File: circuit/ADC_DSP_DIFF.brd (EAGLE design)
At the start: 61 x 76.8 mm, 79 parts, among them IC1 REG1117, IC3 STM32F40XRXT6, IC4 CS4272, Q1 8MHz, Q2 24.576MHz

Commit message: - скомпилировали под Linux
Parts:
- moved C21 8.89 mm to (12.7, 27.9), flipped to the bottom
- moved C23 8.89 mm to (12.7, 25.4), flipped to the bottom
- moved C3 8.89 mm to (12.7, 33.0), flipped to the bottom
- moved C4 8.89 mm to (12.7, 30.5), flipped to the bottom
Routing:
- net GND: track 438.3 -> 418.8 mm
- net N$46: track 3.81 -> 0.00 mm
- net N$43: track 3.81 -> 0.00 mm
- net SW_A: track 9.08 -> 6.45 mm, vias 1 -> 0
- net N$45: track 2.54 -> 0.00 mm
- net N$44: track 2.54 -> 0.00 mm
- net N$27: track 2.54 -> 0.00 mm
- net N$25: track 2.54 -> 0.00 mm
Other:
- board size 61 x 76.8 mm -> 50 x 76.8 mm
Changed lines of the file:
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@@
 <grid distance="0.635" unitdist="mm" unit="mm" style="lines" multiple="1" display="no" altdistance="0.125" altunitdist="mm" altunit="mm"/>
 <layers>
-<layer number="1" name="Top" color="4" fill="1" visible="yes" active="yes"/>
+<layer number="1" name="Top" color="4" fill="1" visible="no" active="yes"/>
 <layer number="16" name="Bottom" color="1" fill="1" visible="yes" active="yes"/>
 <layer number="17" name="Pads" color="2" fill="1" visible="yes" active="yes"/>
@@
 <board>
 <plain>
-<wire x1="0" y1="0" x2="60.95" y2="0" width="0" layer="20"/>
-<wire x1="60.95" y1="0" x2="60.95" y2="76.825" width="0" layer="20"/>
-<wire x1="60.95" y1="76.825" x2="0" y2="76.825" width="0" layer="20"/>
+<wire x1="0" y1="0" x2="50" y2="0" width="0" layer="20"/>
+<wire x1="50" y1="0" x2="50" y2="76.825" width="0" layer="20"/>
+<wire x1="50" y1="76.825" x2="0" y2="76.825" width="0" layer="20"/>
 <wire x1="0" y1="76.825" x2="0" y2="0" width="0" layer="20"/>
 </plain>
@@
 <attribute name="OC_FARNELL" value="unknown" x="8.255" y="29.21" size="1.778" layer="28" rot="MR270" display="off"/>
 </element>
-<element name="C3" library="rcl" package="C0805" value="1n" x="3.81" y="33.02" rot="R180"/>
-<element name="C4" library="rcl" package="C0805" value="1n" x="3.81" y="30.48" rot="R180"/>
-<element name="C21" library="rcl" package="C0805" value="1n" x="3.81" y="27.94" rot="R180"/>
-<element name="C23" library="rcl" package="C0805" value="1n" x="3.81" y="25.4" rot="R180"/>
+<element name="C3" library="rcl" package="C0805" value="1n" x="12.7" y="33.02" rot="MR180"/>
+<element name="C4" library="rcl" package="C0805" value="1n" x="12.7" y="30.48" rot="MR180"/>
+<element name="C21" library="rcl" package="C0805" value="1n" x="12.7" y="27.94" rot="MR180"/>
+<element name="C23" library="rcl" package="C0805" value="1n" x="12.7" y="25.4" rot="MR180"/>
 <element name="R23" library="rcl" package="R0603" value="1.5k" x="12.065" y="33.02"/>
 <element name="R24" library="rcl" package="R0603" value="1.5k" x="11.985" y="30.23"/>
@@
 <wire x1="19.685" y1="38.315" x2="17.36" y2="38.315" width="0.4064" layer="1"/>
 <wire x1="17.36" y1="38.315" x2="16.51" y2="37.465" width="0.4064" layer="1"/>
-<wire x1="2.86" y1="25.4" x2="2.86" y2="27.94" width="0.4064" layer="1"/>
-<wire x1="2.86" y1="27.94" x2="2.86" y2="30.48" width="0.4064" layer="1"/>
-<wire x1="2.86" y1="30.48" x2="2.86" y2="33.02" width="0.4064" layer="1"/>
+<wire x1="13.65" y1="25.4" x2="13.65" y2="27.94" width="0" layer="19" extent="1-16"/>
+<wire x1="13.65" y1="27.94" x2="13.65" y2="30.48" width="0" layer="19" extent="1-16"/>
+<wire x1="13.65" y1="30.48" x2="13.65" y2="33.02" width="0" layer="19" extent="1-16"/>
 <wire x1="27.865" y1="25.415" x2="27.865" y2="24.69" width="0.25" layer="1"/>
 <wire x1="27.865" y1="24.69" x2="27.305" y2="24.13" width="0.25" layer="1"/>
@@
 <wire x1="58.42" y1="36.195" x2="55.88" y2="36.195" width="0.4064" layer="1"/>
 <wire x1="47.625" y1="45.72" x2="44.03" y2="45.72" width="0.4064" layer="1"/>
-<wire x1="2.86" y1="33.02" x2="2.86" y2="52.705" width="0.4064" layer="1"/>
+<wire x1="13.65" y1="33.02" x2="2.86" y2="52.705" width="0" layer="19" extent="1-16"/>
 <wire x1="5.08" y1="52.705" x2="2.86" y2="52.705" width="0.4064" layer="1"/>
 <wire x1="17.36" y1="38.315" x2="17.36" y2="40.425" width="0.4064" layer="1"/>
@@
 <polygon width="0.4064" layer="16" isolate="0.4064">
 <vertex x="0" y="77.47"/>
-<vertex x="60.96" y="77.47"/>
-<vertex x="60.96" y="-0.635"/>
-<vertex x="0" y="-0.635"/>
+<vertex x="50" y="77.47"/>
+<vertex x="50" y="0"/>
+<vertex x="0" y="0"/>
 </polygon>
 <polygon width="0.4064" layer="1" isolate="0.4064">
 <vertex x="0" y="77.47"/>
-<vertex x="60.96" y="77.47"/>
-<vertex x="60.96" y="-0.635"/>
-<vertex x="0" y="-0.635"/>
+<vertex x="50" y="77.47"/>
+<vertex x="50" y="0"/>
+<vertex x="0" y="0"/>
 </polygon>
 <wire x1="15.24" y1="20.955" x2="15.24" y2="21.59" width="0.4064" layer="16"/>
@@
 <wire x1="3.81" y1="23.495" x2="3.175" y2="22.86" width="0.4064" layer="16"/>
 <via x="3.175" y="22.86" extent="1-16" drill="0.6" diameter="1.27"/>
-<wire x1="3.175" y1="22.86" x2="3.175" y2="25.085" width="0.4064" layer="1"/>
-<wire x1="3.175" y1="25.085" x2="2.86" y2="25.4" width="0.4064" layer="1"/>
+<wire x1="3.175" y1="22.86" x2="3.175" y2="25.085" width="0" layer="19" extent="1-16"/>
+<wire x1="3.175" y1="25.085" x2="13.65" y2="25.4" width="0.4064" layer="16"/>
 <wire x1="5.715" y1="6.35" x2="5.715" y2="6.985" width="0.4064" layer="1"/>
 <wire x1="5.715" y1="6.985" x2="3.175" y2="9.525" width="0.4064" layer="1"/>
@@
 <wire x1="32.705" y1="59.16" x2="33.655" y2="60.11" width="0.254" layer="16"/>
 </signal>
-<signal name="N$25">
-<wire x1="1.27" y1="0" x2="0" y2="0" width="0.4064" layer="1"/>
-<wire x1="0" y1="0" x2="0" y2="1.27" width="0.4064" layer="1"/>
-</signal>
-<signal name="N$27">
-<wire x1="1.27" y1="0" x2="0" y2="0" width="0.4064" layer="16"/>
-<wire x1="0" y1="0" x2="0" y2="1.27" width="0.4064" layer="16"/>
-</signal>
 <signal name="N$17">
 <contactref element="IC4" pad="1"/>
@@
 <contactref element="C21" pad="1"/>
 <wire x1="11.215" y1="27.94" x2="8.255" y2="27.94" width="0.4064" layer="1"/>
-<wire x1="8.255" y1="27.94" x2="4.76" y2="27.94" width="0.4064" layer="1"/>
+<wire x1="8.255" y1="27.94" x2="11.75" y2="27.94" width="0.4064" layer="16"/>
 </signal>
 <signal name="N$41">
@@
 <contactref element="C23" pad="1"/>
 <wire x1="11.215" y1="25.4" x2="8.255" y2="25.4" width="0.4064" layer="1"/>
-<wire x1="8.255" y1="25.4" x2="4.76" y2="25.4" width="0.4064" layer="1"/>
+<wire x1="11.75" y1="25.4" x2="8.255" y2="25.4" width="0.4064" layer="16"/>
 </signal>
 <signal name="PC3(GPIO)">
@@
 <contactref element="GPIO" pad="1"/>
 <wire x1="11.215" y1="33.02" x2="8.255" y2="33.02" width="0.4064" layer="1"/>
-<wire x1="8.255" y1="33.02" x2="4.76" y2="33.02" width="0.4064" layer="1"/>
-<wire x1="11.215" y1="33.02" x2="11.215" y2="35.345" width="0.3048" layer="1"/>
-<wire x1="11.215" y1="35.345" x2="11.43" y2="35.56" width="0.3048" layer="1"/>
-<via x="11.43" y="35.56" extent="1-16" drill="0.6" diameter="1.27"/>
+<wire x1="8.255" y1="33.02" x2="11.75" y2="33.02" width="0.4064" layer="16"/>
 </signal>
 <signal name="4052_B">
@@
 <wire x1="11.135" y1="30.23" x2="8.505" y2="30.23" width="0.4064" layer="1"/>
 <wire x1="8.505" y1="30.23" x2="8.255" y2="30.48" width="0.4064" layer="1"/>
-<wire x1="8.255" y1="30.48" x2="4.76" y2="30.48" width="0.4064" layer="1"/>
+<wire x1="8.255" y1="30.48" x2="11.75" y2="30.48" width="0.4064" layer="16"/>
 </signal>
 <signal name="N$18">
@@
 <wire x1="0" y1="76.835" x2="0" y2="74.93" width="0.4064" layer="1"/>
 </signal>
-<signal name="N$43">
-<wire x1="59.055" y1="76.835" x2="60.96" y2="76.835" width="0.4064" layer="1"/>
-<wire x1="60.96" y1="76.835" x2="60.96" y2="74.93" width="0.4064" layer="1"/>
-</signal>
-<signal name="N$44">
-<wire x1="59.69" y1="0" x2="60.96" y2="0" width="0.4064" layer="1"/>
-<wire x1="60.96" y1="0" x2="60.96" y2="1.27" width="0.4064" layer="1"/>
-</signal>
-<signal name="N$45">
-<wire x1="59.69" y1="0" x2="60.96" y2="0" width="0.4064" layer="16"/>
-<wire x1="60.96" y1="0" x2="60.96" y2="1.27" width="0.4064" layer="16"/>
-</signal>
-<signal name="N$46">
-<wire x1="59.055" y1="76.835" x2="60.96" y2="76.835" width="0.4064" layer="16"/>
-<wire x1="60.96" y1="76.835" x2="60.96" y2="74.93" width="0.4064" layer="16"/>
-</signal>
 <signal name="N$47">
 <wire x1="1.905" y1="76.835" x2="0" y2="76.835" width="0.4064" layer="16"/>
@@
 </signal>
 <signal name="N$33">
-<via x="58.42" y="74.295" extent="1-16" drill="3.2"/>
+<via x="46.99" y="74.295" extent="1-16" drill="3.2"/>
 </signal>
 <signal name="N$48">
-<via x="57.785" y="2.54" extent="1-16" drill="3.2"/>
+<via x="46.99" y="2.54" extent="1-16" drill="3.2"/>
 <via x="2.54" y="2.54" extent="1-16" drill="3.2"/>
 </signal>

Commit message: - вроде все линии переразвели
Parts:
- removed R13: 1K5(infinity), rcl:R0603
- moved R12 10.5 mm to (41.3, 37.5)
- moved R3 10.5 mm to (41.3, 35.1)
- moved LCD 9.25 mm to (47.0, 17.1)
- moved R20 9.25 mm to (42.5, 24.8)
- moved R21 9.25 mm to (42.5, 17.1)
- moved R4 9.25 mm to (42.5, 12.1)
- moved R5 9.25 mm to (42.5, 22.2)
- moved R6 9.25 mm to (42.5, 27.3)
- moved R7 9.25 mm to (42.5, 19.7)
- moved R1 9.16 mm to (34.3, 54.2), flipped to the top, turned to 180 degrees
- moved USB 8.98 mm to (47.0, 34.9)
- moved C24 7.18 mm to (33.7, 58.4), turned to 180 degrees
- moved Q2 5.99 mm to (34.9, 49.5), flipped to the bottom
- moved C26 5.99 mm to (17.1, 54.5)
- moved C27 5.99 mm to (28.6, 61.0)
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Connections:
- removed net PA10(USB_ON): IC3.43, R13.1
- net D+: no longer R13.2
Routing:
- net GND: track 418.8 -> 367.5 mm, vias 9 -> 11
- net +3V3: track 182.1 -> 208.6 mm, vias 5 -> 3
- net PA10(USB_ON): track 14.7 -> 0.00 mm
- net USB_DP: track 14.4 -> 9.37 mm
- net USB_DM: track 13.9 -> 9.21 mm
- net PB13(TFT_SCK): track 19.6 -> 15.8 mm
- net PB14(TFT_MISO): track 15.3 -> 11.7 mm
- net PB15(TFT_MOSI): track 24.0 -> 21.6 mm
- net PC8(TFT_LED): track 21.6 -> 19.6 mm
- net PC7(TFT_D_C): track 27.3 -> 29.2 mm
- net N$17: track 3.29 -> 5.15 mm, vias 0 -> 1
- net +5V: track 17.2 -> 15.7 mm
- net PB12(TFT_CS): track 25.6 -> 24.1 mm
- net D-: track 4.07 -> 4.92 mm
- net N$12: track 18.0 -> 18.8 mm, vias 0 -> 1
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
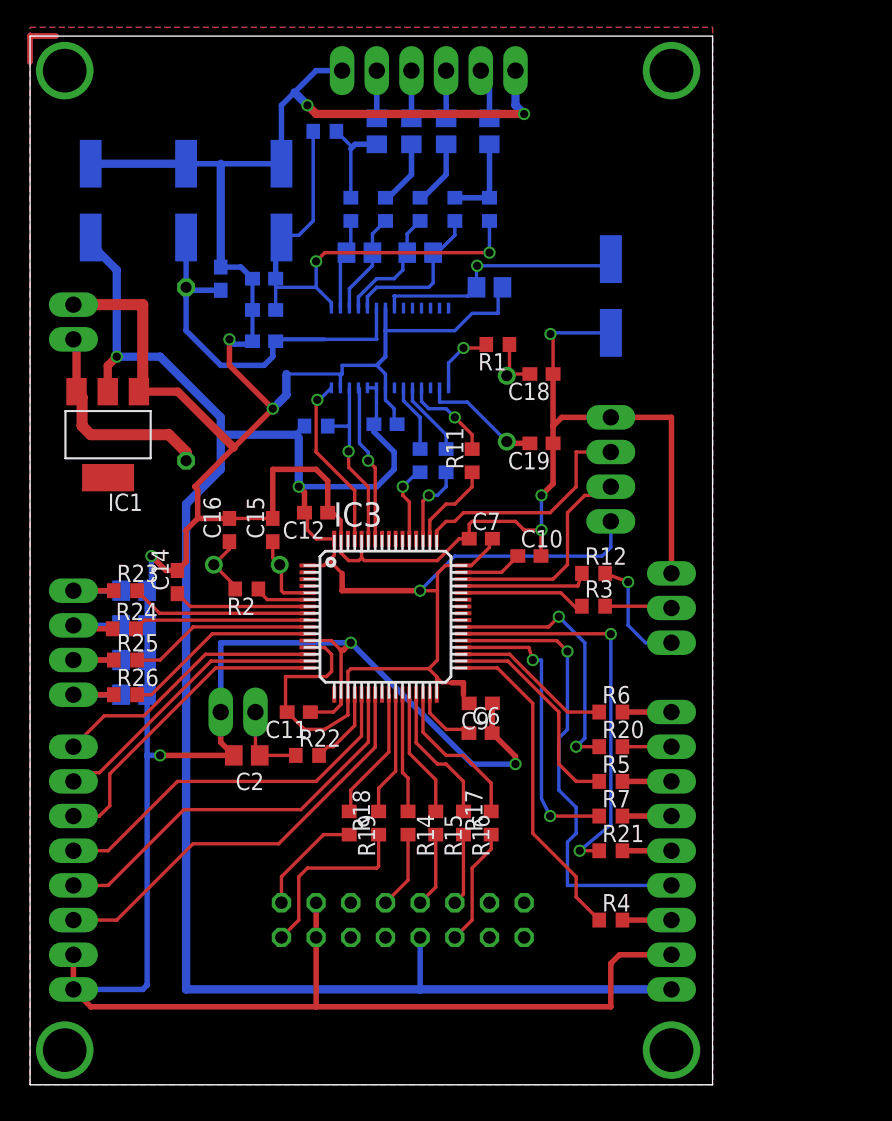
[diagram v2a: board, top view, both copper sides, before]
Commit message: - class VnaCommand, команды, которые можно добавлять в очередь.
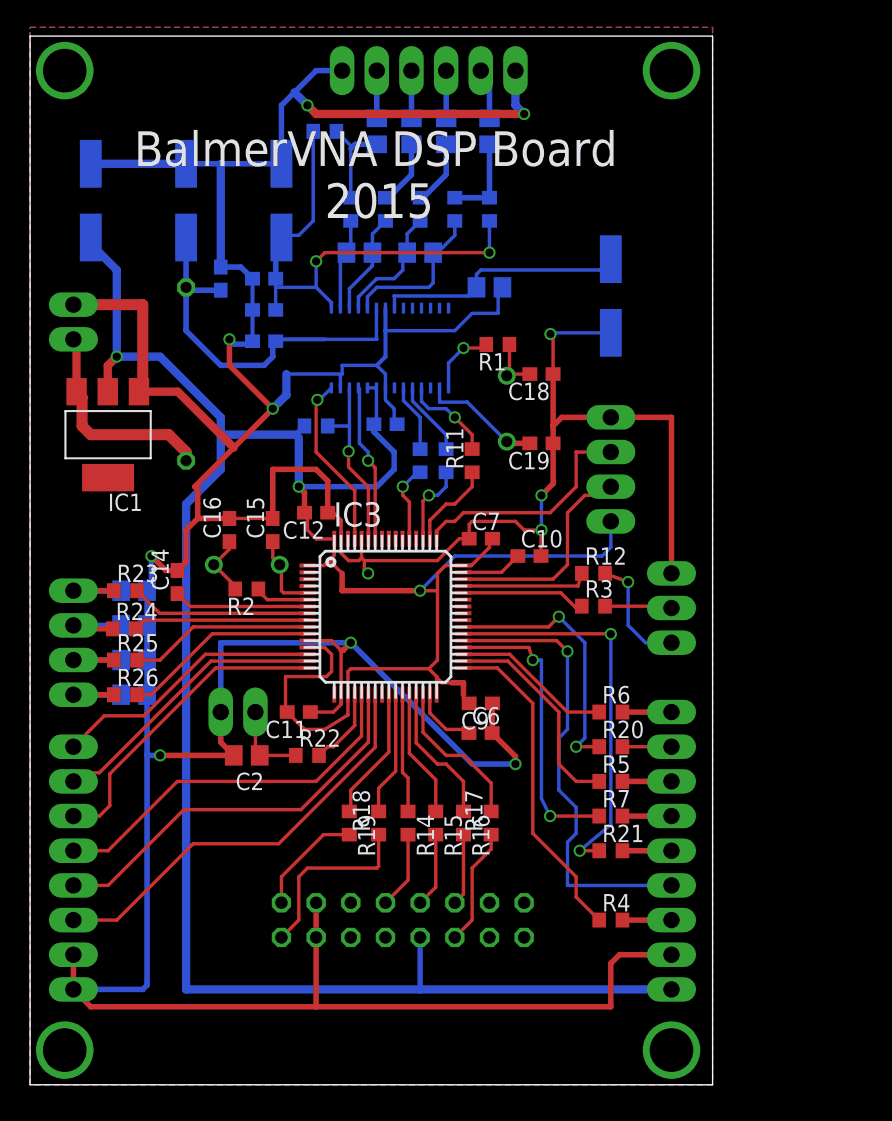
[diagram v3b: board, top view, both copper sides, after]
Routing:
- net N$47: track 3.81 -> 0.00 mm
- net N$42: track 3.81 -> 0.00 mm
- net GND: track 367.5 -> 368.5 mm, vias 11 -> 12
- net N$12: track 18.8 -> 18.5 mm, vias 1 -> 0
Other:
- board text added: "2015"
- board text added: "BalmerVNA DSP Board"
